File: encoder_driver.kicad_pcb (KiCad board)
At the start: 2 copper layers, 21 parts, among them J1 Conn_01x10_Female, J2 Conn_01x10_Female, J3 Conn_01x06, J4 Conn_01x02_Male, Q1 Si2319CDS, U1 AS5045B, U2 AM26LS31CD, U3 AM26LV32xD

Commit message: lots of layout
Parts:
- added REF**: MountingHole_4.3mm_M4, MountingHole:MountingHole_4.3mm_M4, F.Cu at (113.6, 97.0)
- added REF**: MountingHole_4.3mm_M4, MountingHole:MountingHole_4.3mm_M4, F.Cu at (113.6, 55.4)
- added REF**: MountingHole_4.3mm_M4, MountingHole:MountingHole_4.3mm_M4, F.Cu at (77.6, 76.2)
- R3, R4, R5: footprint Resistor_SMD:R_0402_1005Metric -> Resistor_SMD:R_0603_1608Metric
- U1: moved to B.Cu
- moved C4 66.7 mm to (113.5, 62.6), turned to 90 degrees
- moved R1 65.4 mm to (103.8, 62.8), turned to 90 degrees
- moved C1 64.8 mm to (95.6, 72.6), turned to 90 degrees
- moved C6 62.7 mm to (95.6, 75.8), turned to -90 degrees
- moved J4 56.5 mm to (117.2, 87.0)
- moved C2 55.9 mm to (107.2, 82.6), turned to 180 degrees
- moved R2 50.9 mm to (110.4, 82.6), turned to 180 degrees
- moved U1 35.5 mm to (101.6, 76.2), turned to 180 degrees
- moved U2 31.6 mm to (111.8, 76.2), turned to 180 degrees
- moved R4 28.3 mm to (139.4, 70.5), turned to -90 degrees
- moved D1 27.9 mm to (106.5, 65.4), turned to 90 degrees
- moved Q1 27.7 mm to (110.2, 65.4)
- moved J1 25.9 mm to (123.9, 80.3), turned to 180 degrees
- moved C5 24.6 mm to (114.8, 65.4)
- moved R3 24.6 mm to (141.8, 70.5)
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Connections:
- C3 pad 1: V_+5 -> _+5
- C3 pad 2: GND -> _GND
- J2 pad 10: GND -> _GND
- J2 pad 8: GND -> _GND
- J2 pad 9: VIN -> _+5
- J3 pad 1: V_+5 -> _+5
- J3 pad 2: ENC_C -> TEMP
- J3 pad 3: ENC_B -> ENC_C
- J3 pad 4: ENC_A -> ENC_B
- J3 pad 5: TEMP -> ENC_A
- J3 pad 6: GND -> _GND
- R6 pad 2: Net-(U3-Pad16) -> _+5
- U3 pad 16: Net-(U3-Pad16) -> _+5
- U3 pad 8: unconnected-(U3-Pad8) -> _GND
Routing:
- net Net-(J1-Pad8): track 0.00 -> 27.9 mm
- net Net-(J1-Pad7): track 0.00 -> 20.9 mm
- net Net-(J1-Pad5): track 0.00 -> 17.6 mm
- net Net-(J1-Pad6): track 0.00 -> 16.3 mm
- net VIN: track 0.00 -> 13.6 mm
- net Net-(J1-Pad1): track 0.00 -> 12.9 mm
- net GND: track 0.00 -> 12.1 mm, vias 0 -> 9
- net Net-(R2-Pad1): track 0.00 -> 12.1 mm, vias 0 -> 2
- net +5V: track 0.00 -> 11.2 mm, vias 0 -> 2
- net Net-(J1-Pad3): track 0.00 -> 11.0 mm
- net Net-(U1-Pad6): track 0.00 -> 10.7 mm, vias 0 -> 1
- net Net-(U1-Pad4): track 0.00 -> 10.4 mm, vias 0 -> 1
- net Net-(J1-Pad2): track 0.00 -> 8.73 mm
- net Net-(J1-Pad4): track 0.00 -> 7.96 mm
- net Net-(U1-Pad3): track 0.00 -> 6.05 mm, vias 0 -> 1
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- added copper zone on F.Cu, net +5V
- added copper zone on B.Cu, net GND
- added copper zone on F.Cu, net GND
- added copper zone on F.Cu, net VIN
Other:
- board outline added: 56 x 56 mm

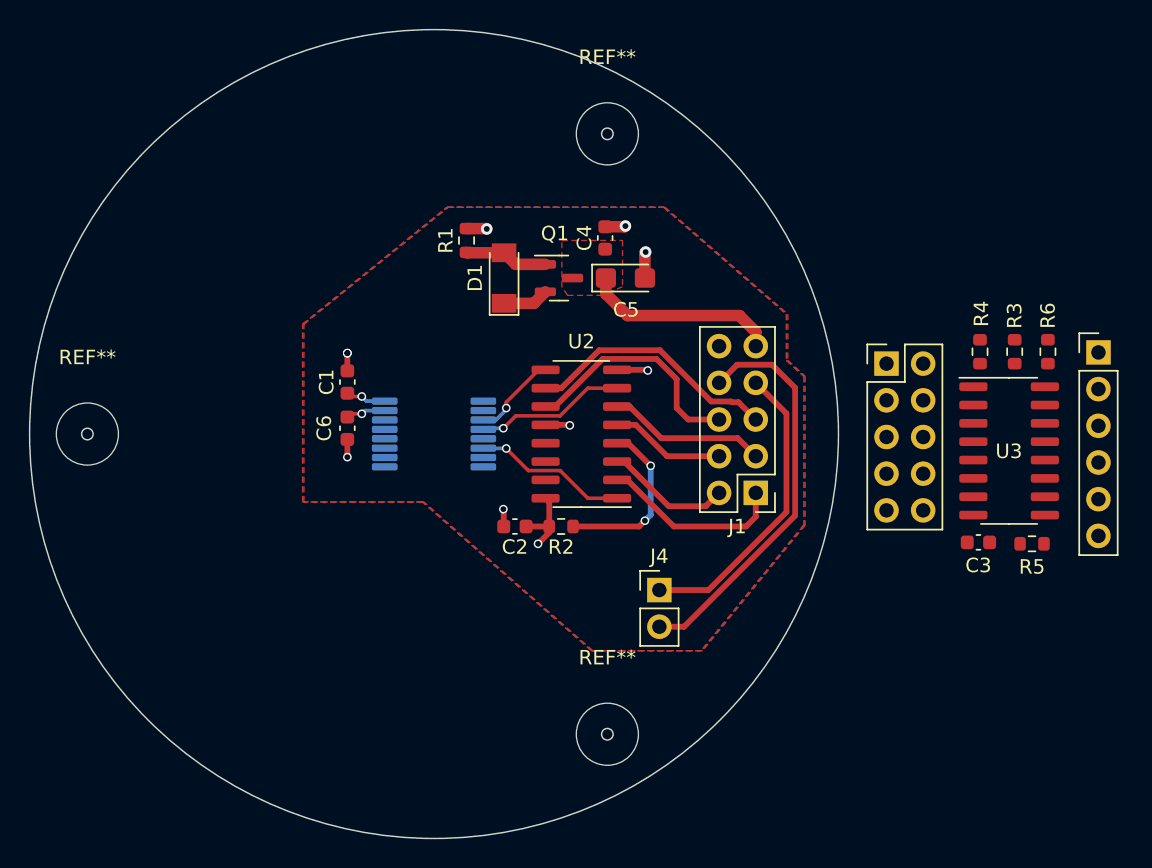
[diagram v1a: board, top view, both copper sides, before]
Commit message: added outline
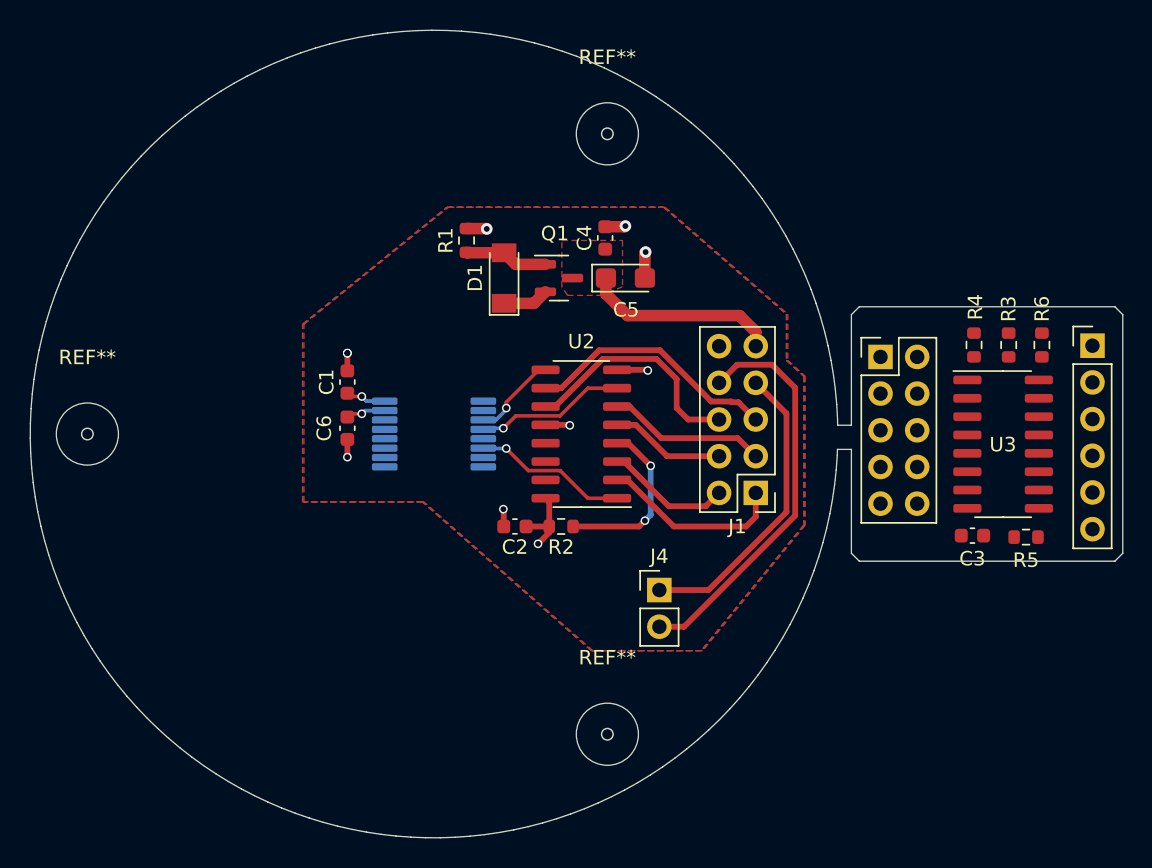
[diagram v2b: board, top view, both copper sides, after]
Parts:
- moved J2 0.62 mm to (132.5, 70.9)
- moved R3 0.62 mm to (141.4, 70.0)
- moved C3 0.62 mm to (138.9, 83.2)
- moved J3 0.62 mm to (147.2, 70.1)
- moved R4 0.62 mm to (139.0, 70.0)
- moved R5 0.62 mm to (142.6, 83.3)
- moved R6 0.62 mm to (143.7, 70.0)
- moved U3 0.62 mm to (141.0, 76.9)
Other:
- board size 56 x 56 mm -> 75.6 x 55.9 mm

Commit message: edits
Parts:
- C5: value 4.7 -> 4.7u
- J3: footprint Connector_PinHeader_2.54mm:PinHeader_1x06_P2.54mm_Vertical -> Connector_JST:my_JST_1x06_P2.00mm_Vertical
- J4: value Conn_01x02_Male -> THRM_IN
- REF** (x3): value MountingHole_4.3mm_M4 -> my_MountingHole_4.3mm_M4; footprint MountingHole:MountingHole_4.3mm_M4 -> MountingHole:my_MountingHole_4.3mm_M4
- moved R5 8.50 mm to (134.1, 83.8)
- moved R3 2.66 mm to (138.7, 70.0), turned to -90 degrees
- moved R4 2.34 mm to (141.3, 70.1)
- moved J3 0.39 mm to (147.2, 70.5), turned to -90 degrees
- moved C3 0.23 mm to (139.1, 83.2)
- moved U3 0.23 mm to (141.2, 76.9)
- moved R6 0.23 mm to (143.9, 70.0)
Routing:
- net TEMP: track 0.00 -> 31.6 mm
- net Net-(J2-Pad5): track 0.00 -> 25.0 mm, vias 0 -> 2
- net Net-(J2-Pad3): track 0.00 -> 24.1 mm, vias 0 -> 1
- net Net-(J2-Pad4): track 0.00 -> 20.2 mm, vias 0 -> 1
- net Net-(J2-Pad6): track 0.00 -> 18.3 mm
- net ENC_B: track 0.00 -> 14.0 mm, vias 0 -> 1
- net ENC_C: track 0.00 -> 13.1 mm, vias 0 -> 1
- net Net-(J2-Pad1): track 0.00 -> 12.5 mm
- net Net-(R6-Pad1): track 0.00 -> 10.1 mm, vias 0 -> 2
- net Net-(J2-Pad2): track 0.00 -> 5.06 mm
- net VIN: track 13.6 -> 17.9 mm
- net ENC_A: track 0.00 -> 3.65 mm
- net _GND: track 0.00 -> 3.44 mm, vias 0 -> 1
- net +5V: track 11.2 -> 9.67 mm, vias 2 -> 1
- net GND: vias 9 -> 8
- added copper zone on F.Cu, net _+5
- added copper zone on B.Cu, net _GND
- removed copper zone on F.Cu, net GND
- removed copper zone on F.Cu, net VIN
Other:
- board size 75.6 x 55.9 mm -> 75.1 x 55.9 mm
- board text added: "+5"
- board text added: "A"
- board text added: "A- A+ B- B+ C- C+ T2 T2 VN GD"
- board text added: "B"
- board text added: "GND"
- board text added: "I"
- board text added: "QS165 HALL ENCODER AS5045B SENSOR V1.0"
- board text added: "T"
- board text added: "VN GD T1 T2 I+ I- B+ B- A+ A-"

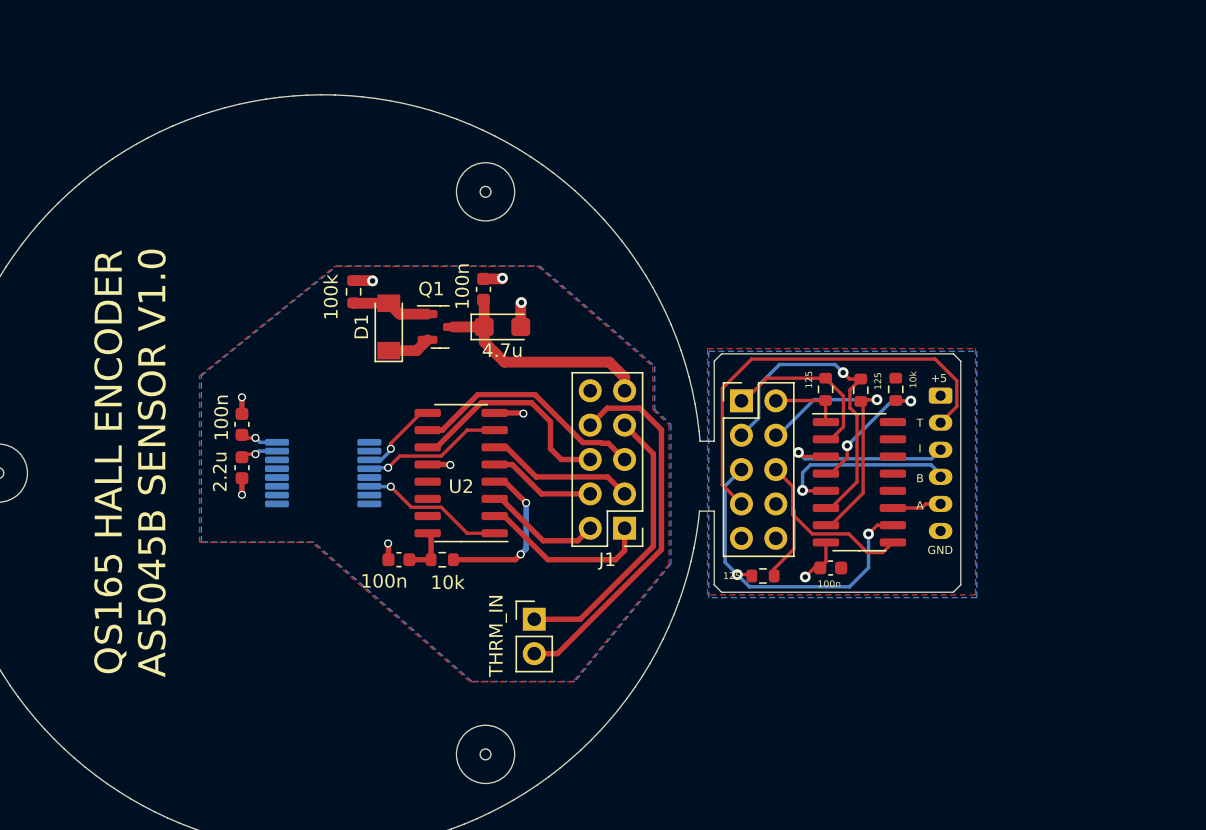
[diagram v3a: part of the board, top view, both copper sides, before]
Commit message: TLE5012 encoder initialization
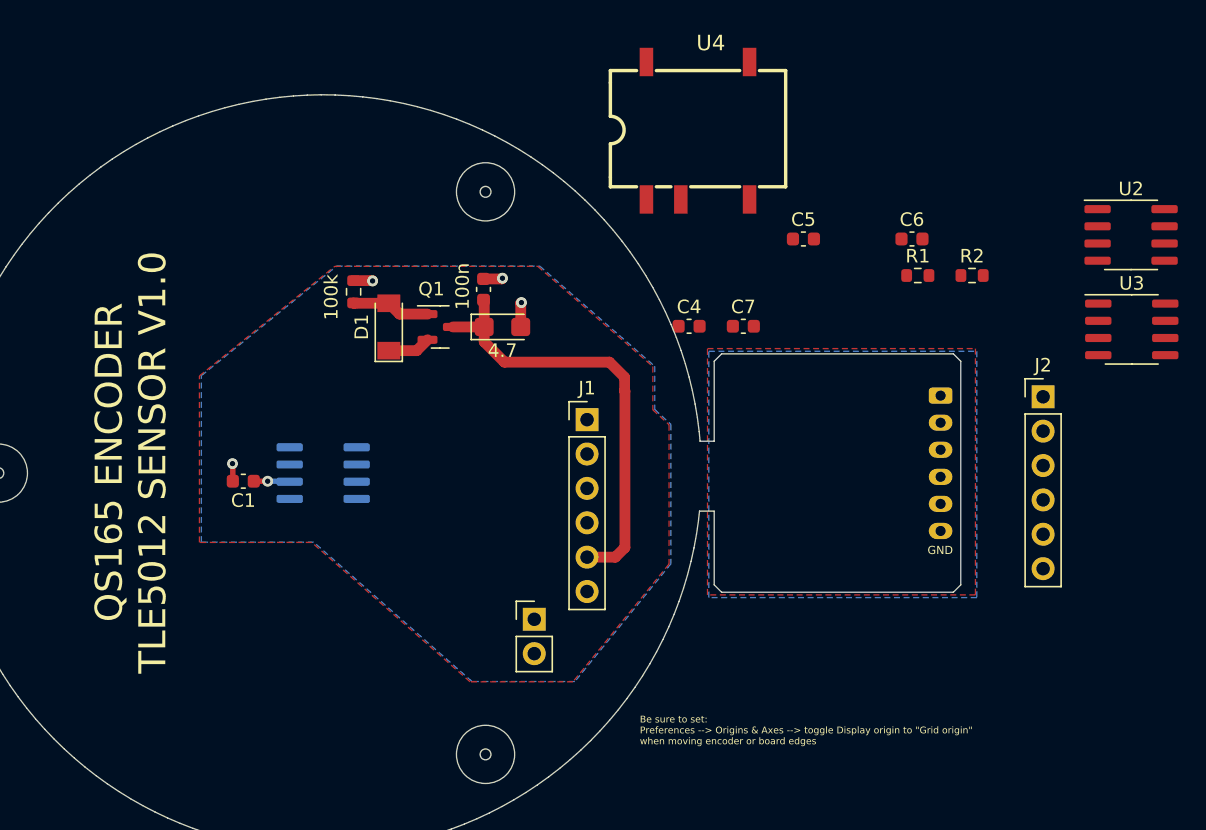
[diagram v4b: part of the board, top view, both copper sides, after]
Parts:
- removed the C2 at (107.2, 82.6)
- removed the C3 at (139.1, 83.2)
- removed the R3 at (138.7, 70.0)
- removed R4, R5: 125, Resistor_SMD:R_0603_1608Metric
- removed R6: 10k, Resistor_SMD:R_0603_1608Metric
- added C4: 100n, Capacitor_SMD:C_0603_1608Metric, F.Cu at (128.6, 65.3)
- added C5: 100n, Capacitor_SMD:C_0603_1608Metric, F.Cu at (137.1, 58.9)
- added C7: 100n, Capacitor_SMD:C_0603_1608Metric, F.Cu at (132.7, 65.3)
- added R1: 10k, Resistor_SMD:R_0603_1608Metric, F.Cu at (145.5, 61.6)
- added U4: B0505T-1W, EASY_EDA:PWRM-SMD_B0505XT-1WR2, F.Cu at (129.3, 50.9)
- C3: renamed from C5; value 4.7u -> 4.7
- C6: value 2.2u -> 100n
- J1, J2: value Conn_01x10_Female -> Conn_01x06_Male; footprint Connector_PinHeader_2.54mm:PinHeader_2x05_P2.54mm_Vertical -> Connector_PinHeader_2.54mm:PinHeader_1x06_P2.54mm_Vertical
- J4: value THRM_IN -> Conn_01x02_Male
- U1: value AS5045B -> TLE5012B; footprint Package_SO:SSOP-16_5.3x6.2mm_P0.65mm -> Package_SO:SOIC-8_3.9x4.9mm_P1.27mm
- U2: value AM26LS31CD -> ISO7321C; footprint Package_SO:SOIC-16_3.9x9.9mm_P1.27mm -> Package_SO:SOIC-8_3.9x4.9mm_P1.27mm
- U3: value AM26LV32xD -> ISO7320C; footprint Package_SO:SOIC-16_3.9x9.9mm_P1.27mm -> Package_SO:SOIC-8_3.9x4.9mm_P1.27mm
- moved U2 52.5 mm to (161.3, 58.6), turned to 0 degrees
- moved C6 52.3 mm to (145.1, 58.9), turned to 0 degrees
- moved R2 44.4 mm to (149.6, 61.6), turned to 0 degrees
- moved U3 23.1 mm to (161.3, 65.6)
- moved J2 22.3 mm to (154.8, 70.6)
- moved J1 8.49 mm to (121.1, 72.2), turned to 0 degrees
- moved C1 4.20 mm to (95.7, 76.8), turned to 180 degrees
- renumbered C4 to C2, R1 to R3
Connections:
- C6 pad 1: Net-(C6-Pad1) -> _+5
- C6 pad 2: GND -> _GND
- J1 pad 1: Net-(J1-Pad1) -> unconnected-(J1-Pad1)
- J1 pad 2: Net-(J1-Pad2) -> unconnected-(J1-Pad2)
- J1 pad 3: Net-(J1-Pad3) -> unconnected-(J1-Pad3)
- J1 pad 4: Net-(J1-Pad4) -> TEMP
- J1 pad 5: Net-(J1-Pad5) -> VIN
- J1 pad 6: Net-(J1-Pad6) -> GND
- J2 pad 1: Net-(J2-Pad1) -> unconnected-(J2-Pad1)
- J2 pad 2: Net-(J2-Pad2) -> unconnected-(J2-Pad2)
- J2 pad 3: Net-(J2-Pad3) -> unconnected-(J2-Pad3)
- J2 pad 4: Net-(J2-Pad4) -> _TEMP
- J2 pad 5: Net-(J2-Pad5) -> _+5
- J2 pad 6: Net-(J2-Pad6) -> _GND
- J3 pad 2: TEMP -> _TEMP
- J3 pad 3: ENC_C -> unconnected-(J3-Pad3)
- J3 pad 4: ENC_B -> unconnected-(J3-Pad4)
- J3 pad 5: ENC_A -> unconnected-(J3-Pad5)
- J4 pad 1: Net-(J1-Pad7) -> unconnected-(J4-Pad1)
- J4 pad 2: Net-(J1-Pad8) -> GND
- R2 pad 1: Net-(R2-Pad1) -> unconnected-(R2-Pad1)
- R2 pad 2: +5V -> unconnected-(R2-Pad2)
- U1 pad 3: Net-(U1-Pad3) -> unconnected-(U1-Pad3)
- U1 pad 4: Net-(U1-Pad4) -> unconnected-(U1-Pad4)
- U1 pad 6: Net-(U1-Pad6) -> +5V
- U1 pad 8: GND -> unconnected-(U1-Pad8)
- U2 pad 1: Net-(U1-Pad6) -> unconnected-(U2-Pad1)
- U2 pad 2: Net-(J1-Pad1) -> unconnected-(U2-Pad2)
- U2 pad 3: Net-(J1-Pad2) -> unconnected-(U2-Pad3)
- U2 pad 4: Net-(R2-Pad1) -> unconnected-(U2-Pad4)
- U2 pad 5: Net-(J1-Pad4) -> unconnected-(U2-Pad5)
- U2 pad 6: Net-(J1-Pad3) -> unconnected-(U2-Pad6)
- U2 pad 7: Net-(U1-Pad4) -> unconnected-(U2-Pad7)
- U2 pad 8: GND -> unconnected-(U2-Pad8)
- U3 pad 1: Net-(J2-Pad2) -> unconnected-(U3-Pad1)
- U3 pad 2: Net-(J2-Pad1) -> unconnected-(U3-Pad2)
- U3 pad 3: ENC_C -> unconnected-(U3-Pad3)
- U3 pad 4: Net-(R6-Pad1) -> unconnected-(U3-Pad4)
- U3 pad 5: ENC_B -> unconnected-(U3-Pad5)
- U3 pad 6: Net-(J2-Pad3) -> unconnected-(U3-Pad6)
- U3 pad 7: Net-(J2-Pad4) -> unconnected-(U3-Pad7)
- U3 pad 8: _GND -> unconnected-(U3-Pad8)
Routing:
- net TEMP: track 31.6 -> 0.00 mm
- net Net-(J1-Pad8): track 27.9 -> 0.00 mm
- net Net-(J2-Pad5): track 25.0 -> 0.00 mm, vias 2 -> 0
- net Net-(J2-Pad3): track 24.1 -> 0.00 mm, vias 1 -> 0
- net Net-(J1-Pad7): track 20.9 -> 0.00 mm
- net Net-(J2-Pad4): track 20.2 -> 0.00 mm, vias 1 -> 0
- net Net-(J2-Pad6): track 18.3 -> 0.00 mm
- net Net-(J1-Pad5): track 17.6 -> 0.00 mm
- net Net-(J1-Pad6): track 16.3 -> 0.00 mm
- net VIN: track 17.9 -> 32.6 mm
- net ENC_B: track 14.0 -> 0.00 mm, vias 1 -> 0
- net ENC_C: track 13.1 -> 0.00 mm, vias 1 -> 0
- net Net-(J1-Pad1): track 12.9 -> 0.00 mm
- net Net-(J2-Pad1): track 12.5 -> 0.00 mm
- net Net-(R2-Pad1): track 12.1 -> 0.00 mm, vias 2 -> 0
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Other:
- board text added: "Be sure to set: Preferences --> Origins & Axes --> toggle Display origin to {dblquote}Grid origin{dblquote} when moving encoder or board edges"
- board text added: "QS165 ENCODER TLE5012 SENSOR V1.0"
- board text removed: "QS165 HALL ENCODER AS5045B SENSOR V1.0"

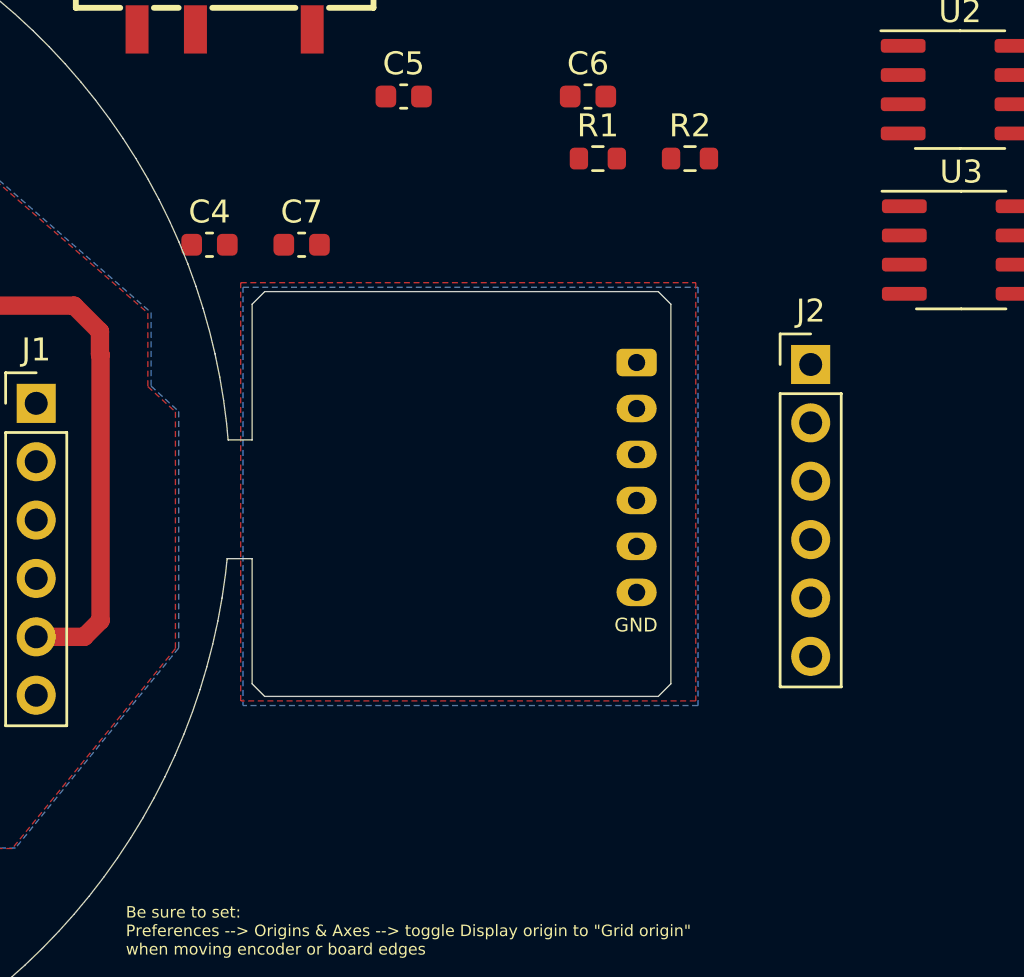
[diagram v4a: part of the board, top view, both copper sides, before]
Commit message: added isolators
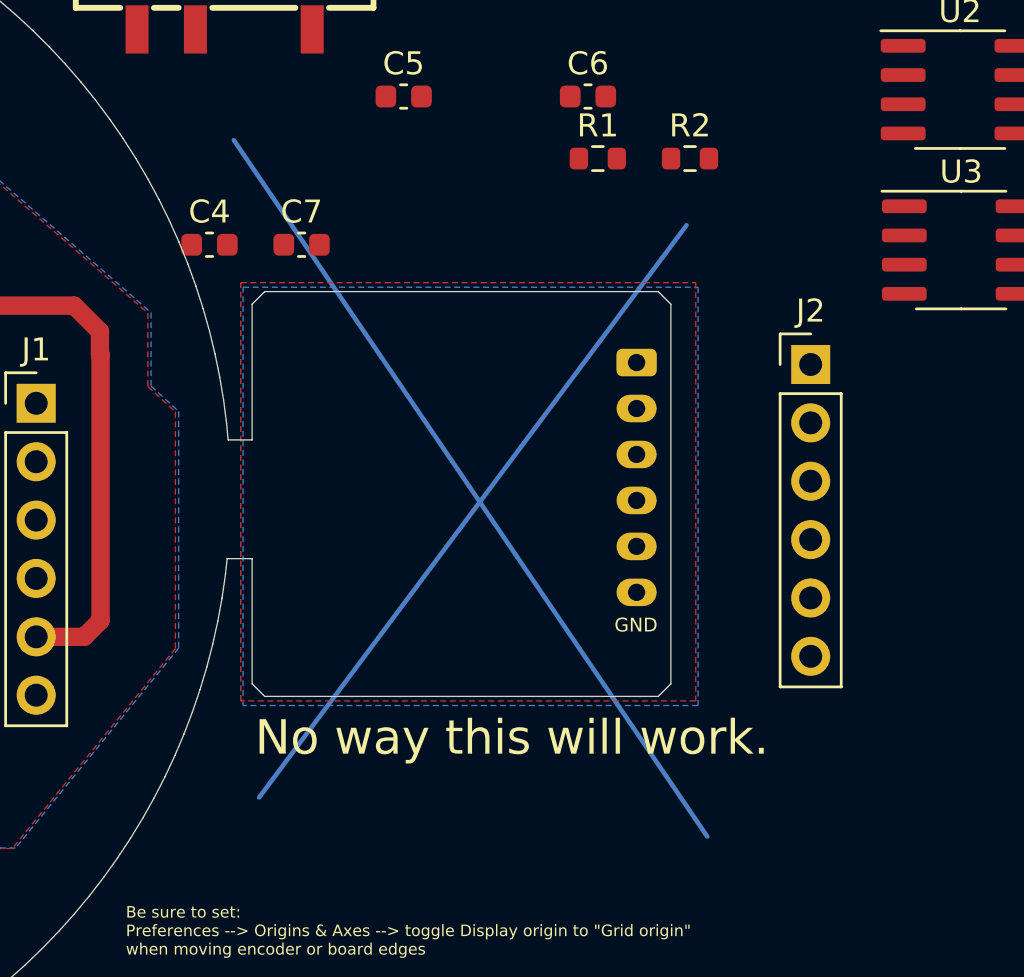
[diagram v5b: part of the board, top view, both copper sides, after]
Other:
- board text added: "No way this will work."
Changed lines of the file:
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@@
     )
   )
+  (gr_line (start 130.8 89.4) (end 149.4 64.5) (layer "B.Cu") (width 0.2))
+  (gr_line (start 129.7 60.8) (end 150.3 91.1) (layer "B.Cu") (width 0.2))
   (gr_rect (start 114.3 83) (end 119.9 67.25) (layer "B.SilkS") (width 0.15) (fill none))
   (gr_circle (center 105.9 72.7) (end 105.6 72.9) (layer "B.SilkS") (width 0.15) (fill none))
@@
     (effects (font (size 0.5 0.5) (thickness 0.05)) (justify left))
   )
+  (gr_text "No way this will work. " (at 141.8 86.8) (layer "F.SilkS")
+    (effects (font (size 1.5 1.5) (thickness 0.3)))
+  )
   (segment (start 96.475 76.8) (end 97.5 76.8) (width 0.4) (layer "F.Cu") (net 1))
